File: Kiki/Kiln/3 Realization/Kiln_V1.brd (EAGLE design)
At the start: 100 x 80 mm, 22 parts, among them T1 2N3904, T2 2N3904, T3 2N3904, T4 2N3904, X1 3.5mm term

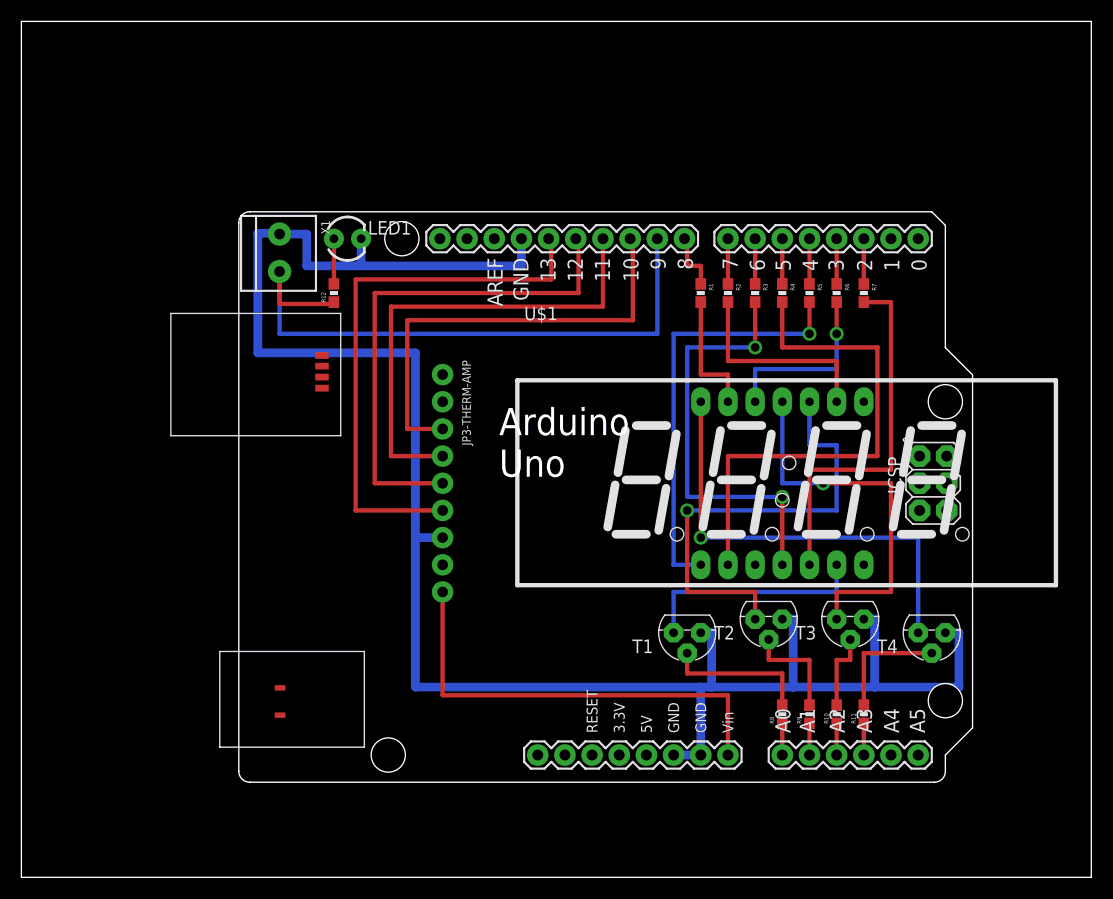
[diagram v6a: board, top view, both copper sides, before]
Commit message: Update: nets are named I had used Wire instead of Net, so I had to rework everything. But it's done.  All nets are named.
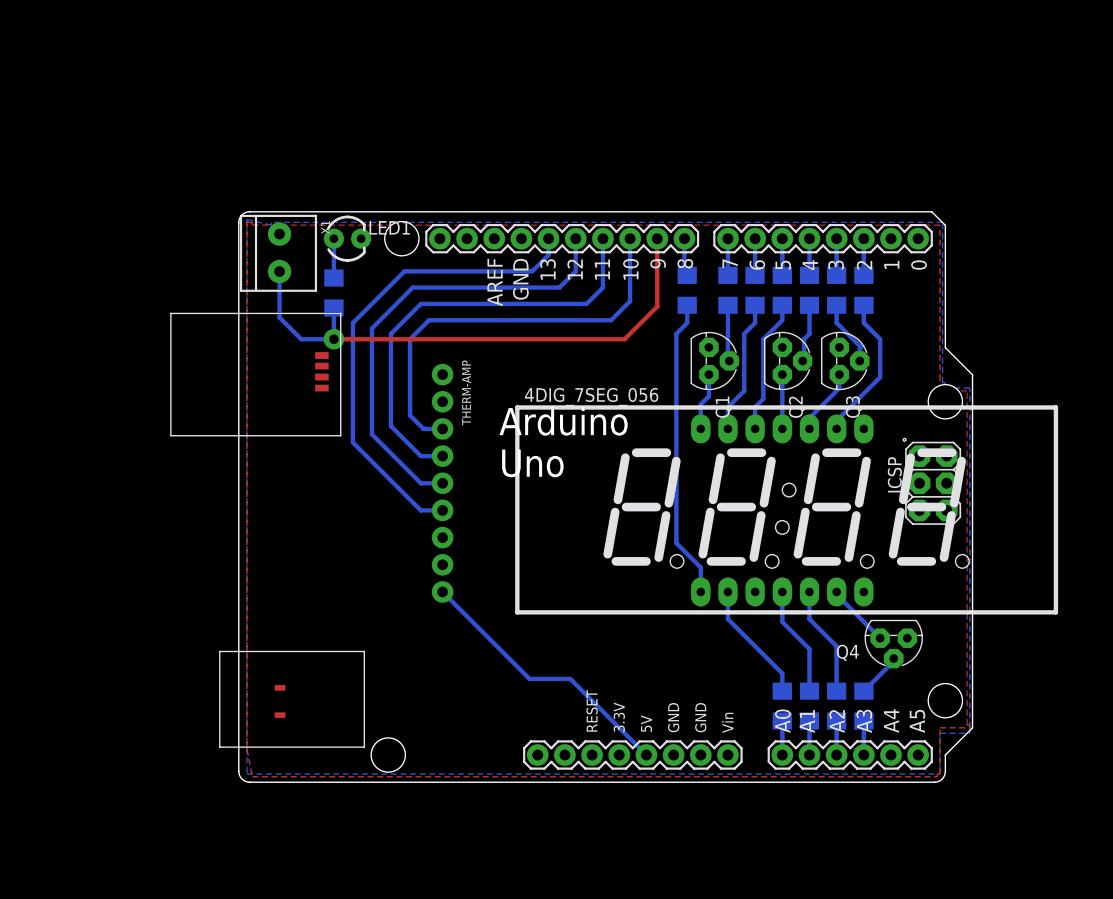
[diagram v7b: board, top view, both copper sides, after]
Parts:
- removed T1, T2, T3, T4: 2N3904, transistor:TO92
- removed U$1: 4DIG_7SEG_056, 7-seg-disp:4DIG_7SEG_056
- added 4DIG_7SEG_056: KW4-56NXBA-P, 7-seg-disp:4DIG_7SEG_056
- added Q1, Q2, Q3, Q4: 2N3904, transistor:TO92
- LED1: value Red -> 559-0102-001F
- R1, R10, R11, R12, R2, R3, R4, R5, R6, R7, R8, R9: device SparkFun-Resistors:0603-RES -> 1-Generic:1206
- THERM-AMP: value 5V -> MAX31856
- moved R11 41.6 mm to (66.0, 54.9), flipped to the bottom, turned to 270 degrees
- moved R10 39.7 mm to (73.7, 54.9), flipped to the bottom, turned to 270 degrees
- moved R9 39.7 mm to (76.2, 54.9), flipped to the bottom, turned to 270 degrees
- moved R6 38.7 mm to (73.7, 16.0), flipped to the bottom, turned to 90 degrees
- moved R5 38.7 mm to (71.1, 16.0), flipped to the bottom, turned to 90 degrees
- moved R7 38.7 mm to (76.2, 16.0), flipped to the bottom, turned to 90 degrees
- moved R1 15.2 mm to (78.7, 54.9), flipped to the bottom
- moved R4 8.89 mm to (62.2, 54.9), flipped to the bottom
- moved R8 7.66 mm to (78.7, 16.0), flipped to the bottom
- moved R2 5.09 mm to (71.1, 54.9), flipped to the bottom
- moved R3 0.25 mm to (68.6, 54.9), flipped to the bottom
- flipped R12 to the bottom
- renumbered JP3-THERM-AMP to THERM-AMP
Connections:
- net !CS renamed CS
- net N$21 renamed R12
- net N$27 renamed DISP-A
- net SDI renamed MOSI
- net SDO renamed MISO
- removed net N$1: R8.2, T1.2
- removed net N$10: R1.2, U$1.13
- removed net N$11: R2.2, U$1.9
- removed net N$12: R3.2, U$1.4
- removed net N$13: R4.2, U$1.2
- removed net N$14: R5.2, U$1.1
- removed net N$15: R6.2, U$1.12
- removed net N$16: R7.2, U$1.5
- removed net N$17: PCB1.A3, R11.1
- removed net N$18: PCB1.A2, R10.1
- removed net N$19: PCB1.A1, R9.1
- removed net N$2: R9.2, T2.2
- removed net N$20: PCB1.A0, R8.1
- removed net N$22: PCB1.7, R2.1
- removed net N$23: PCB1.2, R7.1
- removed net N$24: PCB1.3, R6.1
- removed net N$25: PCB1.4, R5.1
- removed net N$26: PCB1.5, R4.1
- removed net N$3: R10.2, T3.2
- removed net N$31: PCB1.VIN, THERM-AMP.9
- removed net N$4: R11.2, T4.2
- removed net N$5: T1.1, U$1.6
- removed net N$6: T2.1, U$1.10
- removed net N$7: T3.1, U$1.11
- removed net N$8: T4.1, U$1.14
- removed net N$9: PCB1.8, R1.1
- new net A: 4DIG_7SEG_056.13, R3.2
- new net B: 4DIG_7SEG_056.9, R1.2
- new net C: 4DIG_7SEG_056.4, R6.2
- new net D: 4DIG_7SEG_056.2, R5.2
- new net DIG1: 4DIG_7SEG_056.14, Q1.1
- new net DIG2: 4DIG_7SEG_056.11, Q2.1
- new net DIG3: 4DIG_7SEG_056.10, Q3.1
- new net DIG4: 4DIG_7SEG_056.6, Q4.1
- new net DISP-B: PCB1.2, R1.1
- new net DISP-C: PCB1.A1, R6.1
- new net DISP-D: PCB1.A0, R5.1
- new net DISP-DIG1: PCB1.7, R11.1
- new net DISP-DIG2: PCB1.4, R10.1
- new net DISP-DIG3: PCB1.3, R9.1
- new net DISP-DIG4: PCB1.A3, R8.1
- new net DISP-E: PCB1.8, R4.1
- new net DISP-F: PCB1.5, R2.1
- new net DISP-G: PCB1.A2, R7.1
- new net E: 4DIG_7SEG_056.1, R4.2
- new net F: 4DIG_7SEG_056.12, R2.2
- new net G: 4DIG_7SEG_056.5, R7.2
- new net R10: Q2.2, R10.2
- new net R11: Q1.2, R11.2
- new net R8: Q4.2, R8.2
- new net R9: Q3.2, R9.2
- new net VIN: PCB1.5V, THERM-AMP.9
- net GND: now also Q1.3, Q2.3, Q3.3, Q4.3; no longer T1.3, T2.3, T3.3, T4.3
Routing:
- net GND: track 179.8 -> 0.00 mm
- net N$13: track 47.4 -> 0.00 mm
- net N$6: track 43.2 -> 0.00 mm, vias 1 -> 0
- net N$31: track 41.9 -> 0.00 mm
- net N$8: track 41.9 -> 0.00 mm, vias 1 -> 0
- net N$12: track 39.8 -> 0.00 mm, vias 2 -> 0
- net N$14: track 39.8 -> 0.00 mm, vias 1 -> 0
- net N$7: track 35.6 -> 0.00 mm, vias 1 -> 0
- net N$16: track 34.7 -> 0.00 mm
- net E: track 0.00 -> 28.2 mm
- net VIN: track 0.00 -> 25.4 mm
- net N$5: track 21.6 -> 0.00 mm
- net N$11: track 19.5 -> 0.00 mm
- net N$15: track 16.9 -> 0.00 mm, vias 1 -> 0
- net B: track 0.00 -> 13.9 mm
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- added copper zone on layer 1, net GND
- added copper zone on layer 16, net GND
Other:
- board size 100 x 80 mm -> 68.6 x 53.3 mm

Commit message: Added: start button Added pads for soldering the Start Button. Also added the 7seg4dig library, which seems wasn't added. Note: Copy to Library was grayed out.
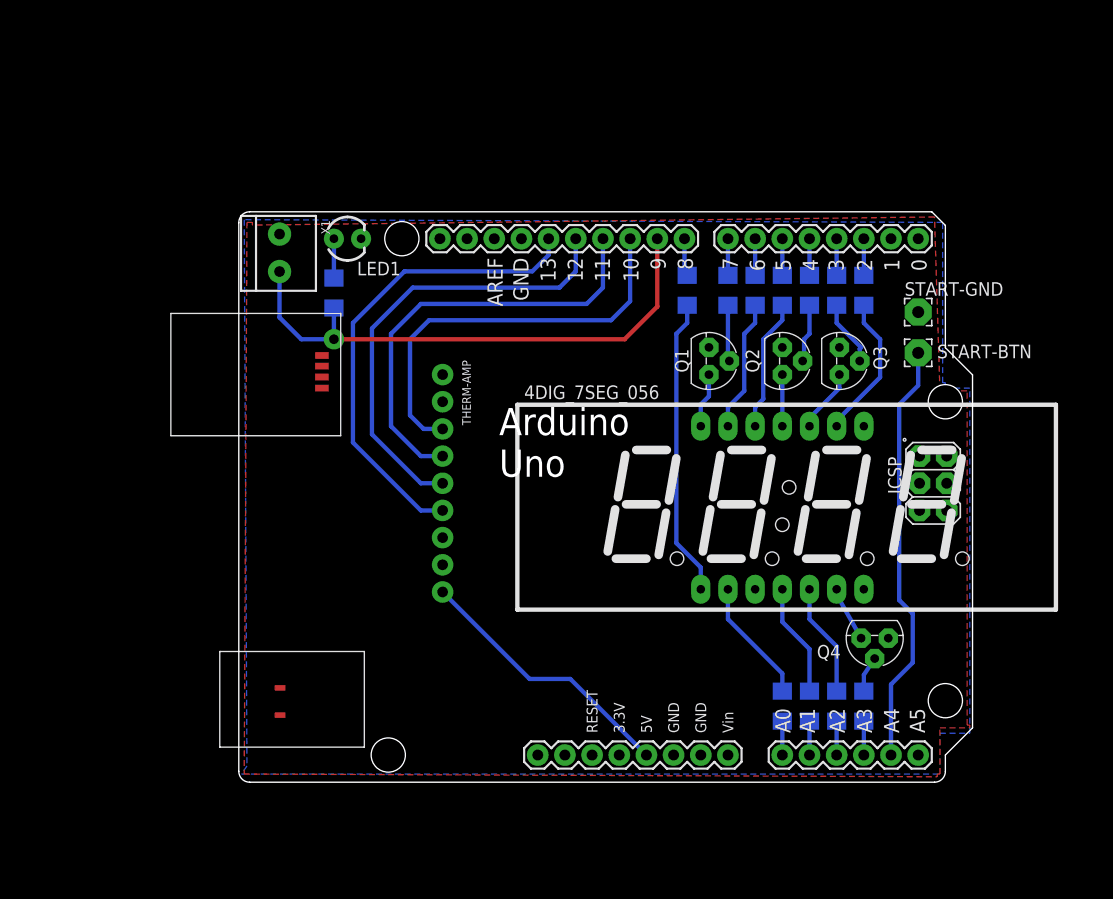
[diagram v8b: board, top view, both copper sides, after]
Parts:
- added START-BTN, START-GND: WIREPAD2,54/1,1, wirepad:2,54/1,1
- moved Q4 1.78 mm to (79.8, 22.4)
- moved 4DIG_7SEG_056 0.25 mm to (71.1, 34.5)
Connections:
- new net START-NET: PCB1.A4, START-BTN.1
- net GND: now also START-GND.1
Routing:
- net START-NET: track 0.00 -> 39.7 mm
- net R8: track 4.20 -> 3.35 mm
- net DIG4: track 6.00 -> 5.17 mm
